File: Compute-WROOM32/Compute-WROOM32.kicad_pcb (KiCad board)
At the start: 4 copper layers, 24.8 x 27.2 mm, 17 parts, among them P1 HiRose-02X15, P4 CONN_01X01, U1 ESP32-WROOM, U2 FT231XS

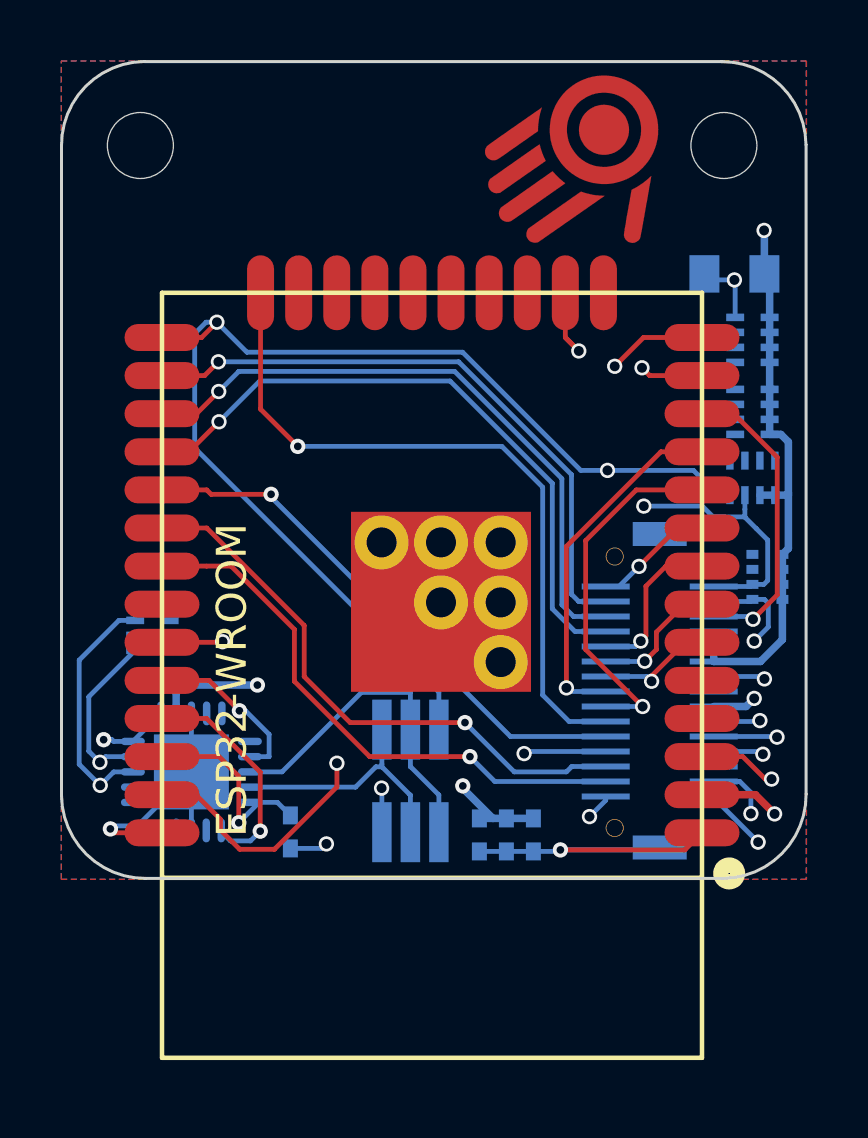
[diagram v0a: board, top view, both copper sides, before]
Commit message: Updated compute module to fix a bug, and to use the WROOM32-U.
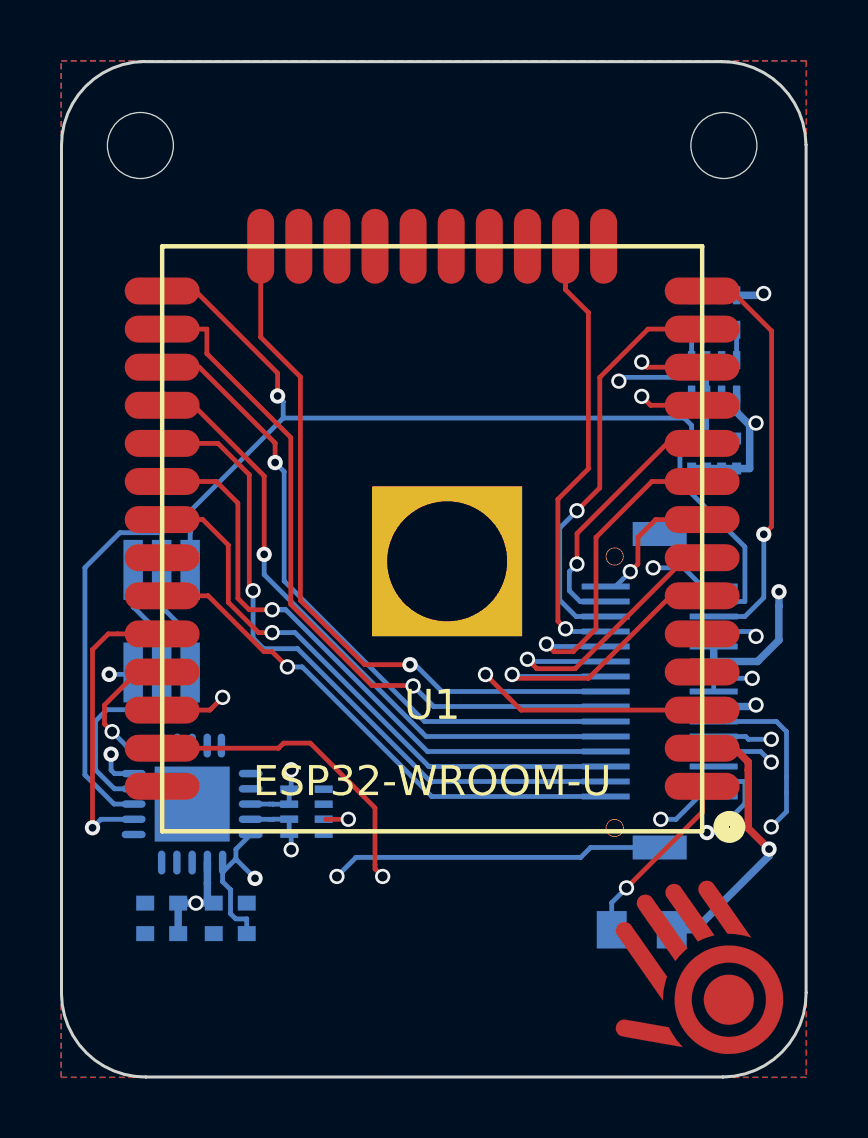
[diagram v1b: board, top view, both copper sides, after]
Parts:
- removed CARY2: 100nF, r2Parts:CapArray_CKCL44
- C2: value IANS_CAP_POLARIZED -> 100uF
- U1: value ESP32-WROOM -> ESP32-WROOM_U; footprint ESP32-footprints-Lib:ESP32-WROOM -> ESP32-footprints-Lib:ESP32-WROOM-U
- moved P4 27.4 mm to (38.9, 48.6), turned to 35 degrees
- moved C2 22.1 mm to (37.2, 46.9)
- moved C3 12.0 mm to (21.2, 47.0), turned to 180 degrees
- moved C1 10.8 mm to (21.2, 46.0), turned to 180 degrees
- moved C5 10.4 mm to (23.5, 46.0), turned to 0 degrees
- moved QA_NPN1 9.85 mm to (21.2, 36.6)
- moved CARY4 7.99 mm to (26.0, 42.9)
- moved RP1 4.48 mm to (39.6, 31.0), turned to 270 degrees
- moved C6 3.94 mm to (23.5, 47.0), turned to 180 degrees
- moved CARY3 3.59 mm to (39.6, 28.4)
- moved CARY1 1.57 mm to (39.6, 26.3), turned to 0 degrees
- moved U1 1.55 mm to (30.2, 36.8)
- moved U2 1.07 mm to (22.2, 42.7), turned to 270 degrees
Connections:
- RP1 pad 7: (no net) -> Net-(RP1-Pad7)
- RP1 pad 8: (no net) -> Net-(RP1-Pad8)
- U1 pad 10: /CPLD_OE -> /SPI1_MISO
- U1 pad 11: /~CPLD_RESET -> /I2C_SDA
- U1 pad 12: /~SHUTDOWN -> /I2C_SCL
- U1 pad 13: /I2C_SDA -> /SPI1_MOSI
- U1 pad 14: /I2C_SCL -> /~SHUTDOWN
- U1 pad 16: /ALERT -> /SPI1_CLK
- U1 pad 17: (no net) -> Net-(U1-Pad17)
- U1 pad 18: (no net) -> Net-(U1-Pad18)
- U1 pad 19: (no net) -> Net-(U1-Pad19)
- U1 pad 20: (no net) -> Net-(U1-Pad20)
- U1 pad 21: (no net) -> Net-(U1-Pad21)
- U1 pad 22: (no net) -> Net-(U1-Pad22)
- U1 pad 23: (no net) -> Net-(U1-Pad23)
- U1 pad 24: /CPLD_EXT_CLK -> /~CPLD_RESET
- U1 pad 26: /SPI1_MISO -> /CPLD_OE
- U1 pad 27: /SPI1_MOSI -> /CPLD_EXT_CLK
- U1 pad 28: /SPI1_CLK -> /SPI1_CS
- U1 pad 29: /SPI1_CS -> /~LED_RESET
- U1 pad 30: /~LED_INT -> /~REQ
- U1 pad 31: /~LED_RESET -> /~LED_INT
- U1 pad 32: (no net) -> Net-(U1-Pad32)
- U1 pad 33: /~REQ -> /ALERT
- U1 pad 4: (no net) -> Net-(U1-Pad4)
- U1 pad 5: (no net) -> Net-(U1-Pad5)
- U1 pad 8: /SPI2_MOSI -> /IRQ_WAKEUP
- U1 pad 9: /IRQ_WAKEUP -> /SPI2_MOSI
- U2 pad 14: (no net) -> Net-(U2-Pad14)
- U2 pad 15: (no net) -> Net-(U2-Pad15)
- U2 pad 16: (no net) -> Net-(U2-Pad16)
- U2 pad 2: (no net) -> Net-(U2-Pad2)
- U2 pad 4: (no net) -> Net-(U2-Pad4)
- U2 pad 5: (no net) -> Net-(U2-Pad5)
- U2 pad 6: (no net) -> Net-(U2-Pad6)
- U2 pad 7: (no net) -> Net-(U2-Pad7)
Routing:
- net /PIN_0: track 53.0 -> 35.7 mm, vias 3 -> 1
- net /USB_D-: track 34.1 -> 17.5 mm
- net /CHIP_PU: track 37.8 -> 51.1 mm, vias 3 -> 4
- net /USB_D+: track 34.1 -> 22.2 mm
- net /~CPLD_RESET: track 11.9 -> 23.8 mm
- net /SPI1_MISO: track 20.6 -> 8.79 mm
- net /CPLD_OE: track 12.1 -> 23.7 mm
- net /SPI1_MOSI: track 21.2 -> 13.8 mm
- net /FTDI_RESET: track 15.1 -> 22.0 mm, vias 2 -> 3
- net /SPI1_CLK: track 21.7 -> 15.0 mm
- net /SPI2_CLK: track 4.70 -> 10.7 mm
- net Net-(QA_NPN1-Pad2): track 11.5 -> 17.0 mm
- net /SPI2_MOSI: track 6.28 -> 11.4 mm
- net /I2C_SDA: track 19.0 -> 23.7 mm
- net /~REQ: track 16.4 -> 20.8 mm, vias 2 -> 1
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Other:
- board size 24.8 x 27.2 mm -> 24.8 x 33.9 mm
- board text added: "IO21: BATT_IRQ IO23: BATT_ISEL IO19: ~LED_INT IO05: ~LED_RESET IO02: ~CPLD_RESET IO04: CPLD_OE IO12: CPLD_PWR IO16: CPLD_EXT_CLK IO32: CPLD_IRQ"
- board text added: "IO35: ~SPI2_CS IO34: SPI2_CLK IO33: SPI2_MOSI IO18: ~REQ IO17: ~SPI1_CS IO13: SPI1_CLK IO14: SPI1_MOSI IO25: SPI1_MISO IO26: I2C_SDA IO27: I2C_SCL"
- board text removed: "IO05: SPI1_CS IO17: SPI1_CLK IO16: SPI1_MOSI IO04: SPI1_MISO IO02: CPLD_CLK IO33: CPLD_IRQ IO27: CPLD_PWR IO25: CPLD_OE IO12: I2C_SCL IO14: I2C_SDA"
- board text removed: "IO35: SPI2_CS IO34: SPI2_CLK IO32: SPI2_MOSI IO21: ~REQ IO26: ~CPLD_RESET IO33: CPLD_IRQ IO18: ~LED_IRQ IO19: ~LED_RESET IO13: BATT_IRQ IO23: ISEL"

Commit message: Compute module will now take either WROOM32 module.
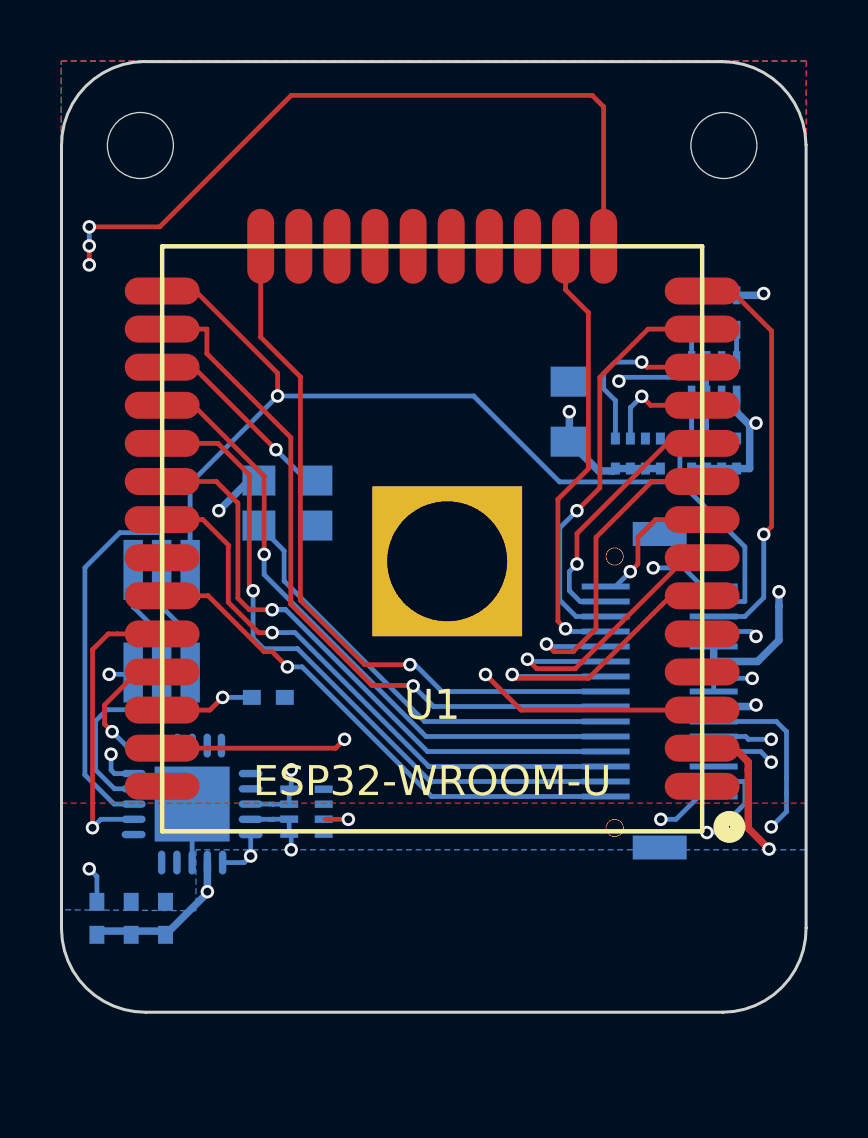
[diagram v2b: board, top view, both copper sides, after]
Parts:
- removed P4: CONN_01X01, manuvr_logo:ManuvrLogo
- added RP2: 15k, r2Parts:RES_4_EXBN8V, B.Cu at (37.1, 31.0)
- added U3: ASTMLP, r2Parts:ASTMLPD, B.Cu at (25.4, 32.6)
- moved C2 17.4 mm to (34.8, 29.6), turned to 90 degrees
- moved C6 7.98 mm to (24.8, 39.1), turned to 0 degrees
- moved C5 4.47 mm to (19.1, 46.5), turned to 90 degrees
- moved C3 1.14 mm to (20.2, 46.5), turned to 90 degrees
- moved C1 0.52 mm to (21.3, 46.5), turned to 90 degrees
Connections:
- U1 pad 27: /CPLD_EXT_CLK -> Net-(U1-Pad27)
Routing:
- net /VCC0: track 22.4 -> 49.8 mm, vias 4 -> 6
- net GND: track 26.3 -> 37.3 mm, vias 5 -> 7
- net /CPLD_EXT_CLK: track 22.2 -> 14.9 mm, vias 1 -> 0
- net Net-(U1-Pad27): track 0.00 -> 6.69 mm, vias 0 -> 1
- net /FTDI_RESET: track 22.0 -> 16.1 mm
- net /I2C_SCL: track 19.9 -> 23.6 mm
- net /ISEL: track 30.0 -> 27.6 mm
- net /USB_D+: track 22.2 -> 20.6 mm
- net /USB_D-: track 17.5 -> 18.9 mm
- net /PIN_0: track 35.7 -> 36.6 mm
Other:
- board size 24.8 x 33.9 mm -> 24.8 x 31.7 mm
- net class Default: via_dia 0.51 -> 0.45; via_drill 0.33 -> 0.26
- net class GND: via_dia 0.51 -> 0.45; via_drill 0.33 -> 0.26
- net class High-Current: via_dia 0.51 -> 0.45; via_drill 0.33 -> 0.26
- board text added: "ESP32 Compute r2 2019.01.26 manuvr.io"
- board text added: "IO21: BATT_IRQ IO23: BATT_ISEL IO19: ~LED_INT IO05: ~LED_RESET IO26: I2C_SDA IO27: I2C_SCL IO02: ~CPLD_RESET IO04: CPLD_OE IO12: CPLD_PWR IO16: CPLD_EXT_CLK IO32: CPLD_IRQ"
- board text added: "IO35: ~SPI2_CS IO34: SPI2_CLK IO33: SPI2_MOSI IO18: ~REQ IO17: ~SPI1_CS IO13: SPI1_CLK IO14: SPI1_MOSI IO25: SPI1_MISO"
- board text added: "This is the proximal edge of the ESP32 antenna."
- board text removed: "ESP32 Compute r2 manuvr.io"
- board text removed: "IO21: BATT_IRQ IO23: BATT_ISEL IO19: ~LED_INT IO05: ~LED_RESET IO02: ~CPLD_RESET IO04: CPLD_OE IO12: CPLD_PWR IO16: CPLD_EXT_CLK IO32: CPLD_IRQ"
- board text removed: "IO35: ~SPI2_CS IO34: SPI2_CLK IO33: SPI2_MOSI IO18: ~REQ IO17: ~SPI1_CS IO13: SPI1_CLK IO14: SPI1_MOSI IO25: SPI1_MISO IO26: I2C_SDA IO27: I2C_SCL"
